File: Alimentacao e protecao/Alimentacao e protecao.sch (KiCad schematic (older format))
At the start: 18 parts, among them J1 PinoCheckBateriaVcc, J2 PinoCheckBateriaGND, J3 Conn_01x01_MedidorBateriaVcc, J4 Conn_01x01_MedidorBateriaGnd, Q1 BC548, Q2 BC548, SW1 SW_ON/OFF

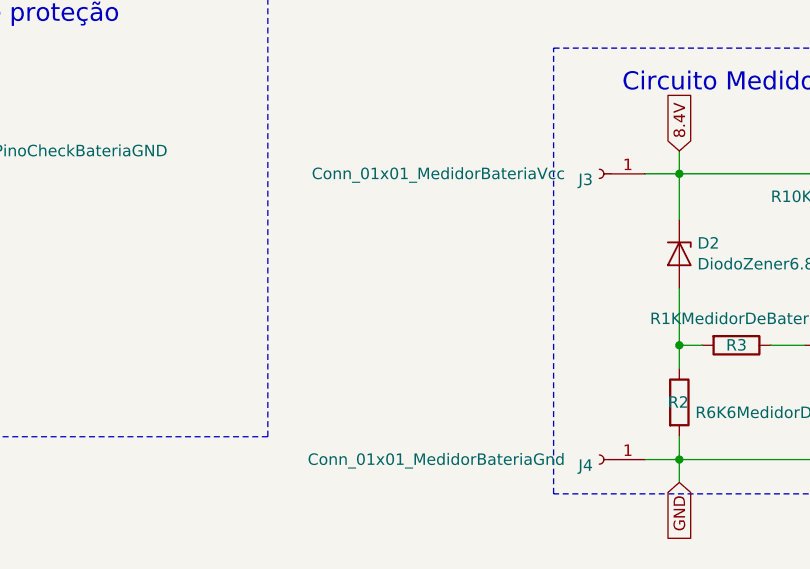
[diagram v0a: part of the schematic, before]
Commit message: Distribuição dos compenentes praticamente concluída, quase pronta para root.
Placa Central: 5VArduino(pino 15) colocado no pino 16, enquanto o sensorEsq(pino 16) foi colocado no pino 15 para
facilitar o root; Adicionado na placa central os pads de conexao das alimentacoes provenientes do circuito de
alimentacao; Label '5V' substituída por '5VArduino' - decisão a ser revisada; Pads de solda trocados por pads maiores
por questoes de corrente alta (pinos de alimentacao). *Placa de Alimentação: Nome de dois pinos da placa de alimentação
modificados. Pads de solda trocados por pads maiores por questoes de corrente alta (pinos de alimentacao).
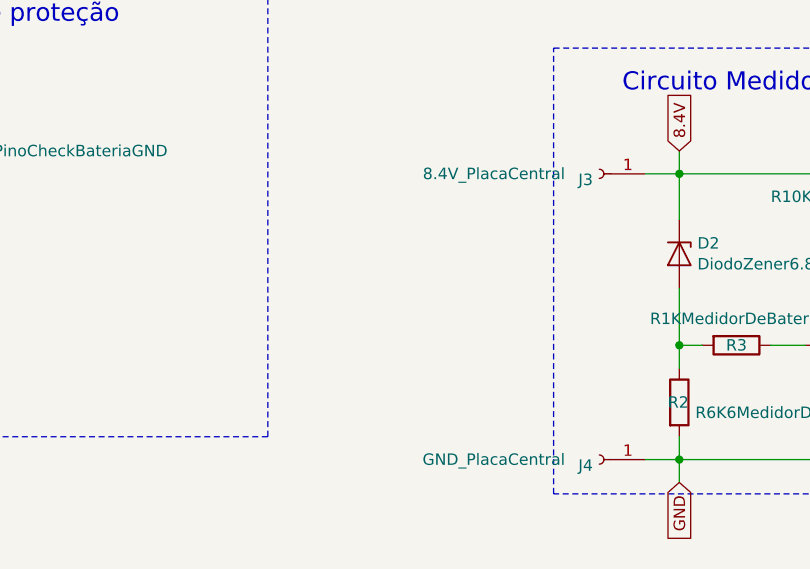
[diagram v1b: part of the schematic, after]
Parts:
- J3: value Conn_01x01_MedidorBateriaVcc -> 8.4V_PlacaCentral; footprint Connector_PinSocket_2.54mm:PinSocket_1x01_P2.54mm_Vertical -> Connector_Wire:SolderWirePad_1x01_Drill1.2mm
- J4: value Conn_01x01_MedidorBateriaGnd -> GND_PlacaCentral; footprint Connector_PinSocket_2.54mm:PinSocket_1x01_P2.54mm_Vertical -> Connector_Wire:SolderWirePad_1x01_Drill1.2mm
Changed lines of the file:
@@
 EESchema Schematic File Version 4
+LIBS:Alimentacao e protecao-cache
 EELAYER 26 0
 EELAYER END
@@
 P 6450 2150
 F 0 "J3" H 6478 2176 50  0000 L CNN
-F 1 "Conn_01x01_MedidorBateriaVcc" H 6600 2150 50  0000 L CNN
-F 2 "Connector_PinSocket_2.54mm:PinSocket_1x01_P2.54mm_Vertical" H 6450 2150 50  0001 C CNN
+F 1 "8.4V_PlacaCentral" H 6600 2150 50  0000 L CNN
+F 2 "Connector_Wire:SolderWirePad_1x01_Drill1.2mm" H 6450 2150 50  0001 C CNN
 F 3 "~" H 6450 2150 50  0001 C CNN
 	1    6450 2150
@@
 P 6450 3400
 F 0 "J4" H 6478 3426 50  0000 L CNN
-F 1 "Conn_01x01_MedidorBateriaGnd" H 6600 3400 50  0000 L CNN
-F 2 "Connector_PinSocket_2.54mm:PinSocket_1x01_P2.54mm_Vertical" H 6450 3400 50  0001 C CNN
+F 1 "GND_PlacaCentral" H 6600 3400 50  0000 L CNN
+F 2 "Connector_Wire:SolderWirePad_1x01_Drill1.2mm" H 6450 3400 50  0001 C CNN
 F 3 "~" H 6450 3400 50  0001 C CNN
 	1    6450 3400
